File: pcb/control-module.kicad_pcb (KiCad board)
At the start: 2 copper layers, 78.7 x 69.9 mm, 175 parts, among them J1 Screw_Terminal_01x06, J2 Conn_01x07_Pin, J3 USB_C_Receptacle_USB2.0_16P, J4 Micro_SD_Card, J5 Conn_ST_STDC14, J6 Conn_Coaxial, Q1 SiS454DN, Q2 SiS454DN, SW1 SW_DIP_x04, SW2 SW_DIP_x04, U1 TPS2116DRL, U2 USBLC6-2SC6, U3 STM32U545RETxQ, U4 MS5607-02BA, U5 LSM6DSL, U6 MCP73831-2-OT, U7 MIC5504-3.3YM5, U9 STM32WL55CCUx

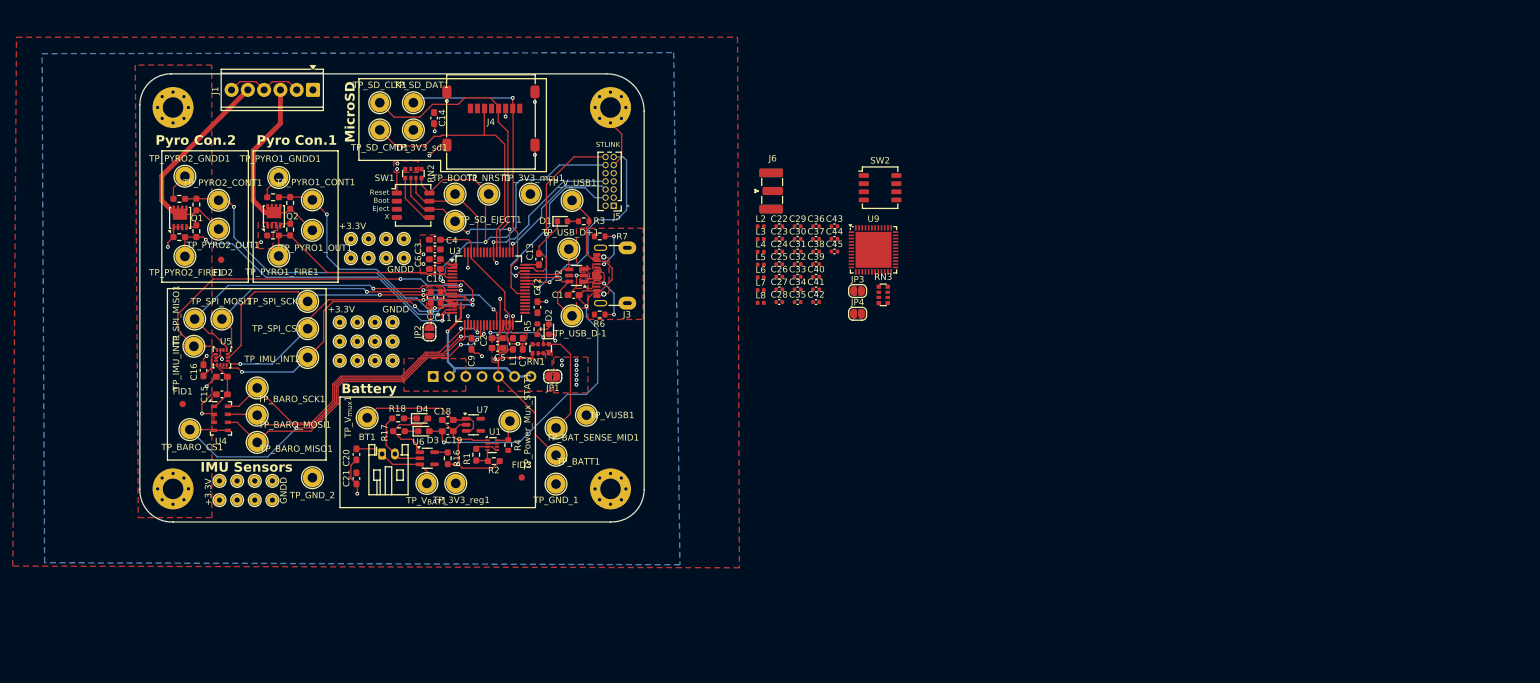
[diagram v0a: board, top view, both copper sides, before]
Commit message: Updated parts
Updated parts, most should be included at this point. Layout is not complete.
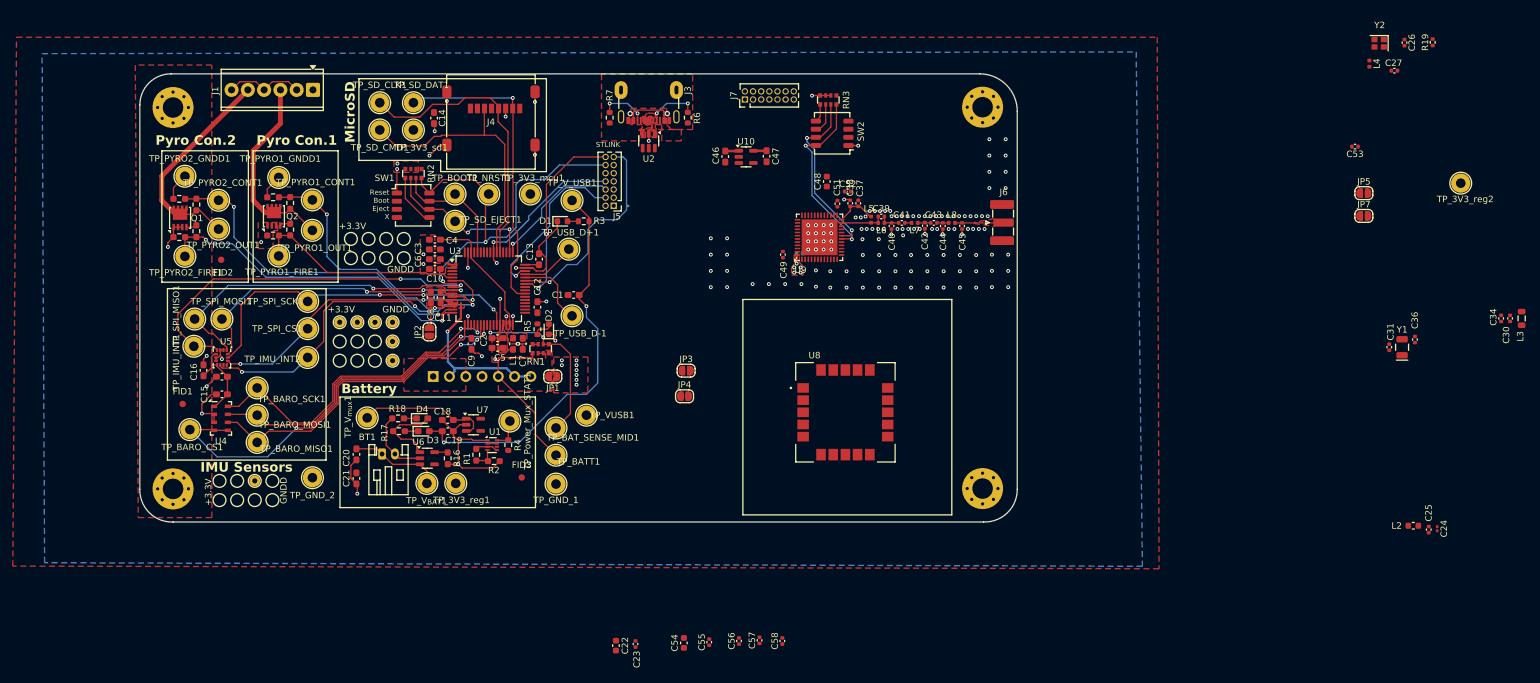
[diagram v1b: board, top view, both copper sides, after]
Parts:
- removed ? (x21): , 
- removed C28, C29, C32, C33, C35: C, Capacitor_SMD:C_0402_1005Metric
- added C46: 1uF, Capacitor_SMD:C_0603_1608Metric_Pad1.08x0.95mm_HandSolder, F.Cu at (206.7, 32.9)
- added C47: 1uF, Capacitor_SMD:C_0603_1608Metric_Pad1.08x0.95mm_HandSolder, F.Cu at (213.1, 32.9)
- added C48: 4.7uF, Capacitor_SMD:C_0603_1608Metric, F.Cu at (222.5, 36.8)
- added C49: 100nF, Capacitor_SMD:C_0402_1005Metric, F.Cu at (215.7, 48.2)
- added C50: 33pF, Capacitor_SMD:C_0402_1005Metric, B.Cu at (218.2, 48.0)
- added C51: 33pF, Capacitor_SMD:C_0402_1005Metric, F.Cu at (224.2, 40.2)
- added C52: 100nF, Capacitor_SMD:C_0402_1005Metric, F.Cu at (225.8, 38.4)
- added C53: 33pF, Capacitor_SMD:C_0402_1005Metric, F.Cu at (304.9, 31.4)
- added C54: 4.7uF, Capacitor_SMD:C_0603_1608Metric, F.Cu at (200.2, 108.8)
- added C55: 100nF, Capacitor_SMD:C_0402_1005Metric, F.Cu at (204.2, 108.7)
- added C56: 100nF, Capacitor_SMD:C_0402_1005Metric, F.Cu at (208.8, 108.5)
- added C57: 100nF, Capacitor_SMD:C_0402_1005Metric, F.Cu at (212.0, 108.4)
- added C58: 100nF, Capacitor_SMD:C_0402_1005Metric, F.Cu at (215.6, 108.5)
- added J7: Conn_ST_STDC14, Connector_PinHeader_1.27mm:PinHeader_2x07_P1.27mm_Vertical, F.Cu at (209.7, 24.0)
- added JP5: ~, Jumper:SolderJumper-2_P1.3mm_Open_RoundedPad1.0x1.5mm, F.Cu at (306.3, 38.6)
- added JP7: SolderJumper_2_Open, Jumper:SolderJumper-2_P1.3mm_Open_RoundedPad1.0x1.5mm, F.Cu at (306.3, 42.2)
- added R19: 220R, Resistor_SMD:R_0402_1005Metric, F.Cu at (317.0, 15.1)
- added TP_3V3_reg2: TestPoint, TestPoint:TestPoint_Loop_D2.54mm_Drill1.5mm_Beaded, F.Cu at (321.4, 37.0)
- added U10: MIC5504-3.3YM5, Package_TO_SOT_SMD:SOT-23-5, F.Cu at (209.9, 33.0)
- added U8: SAM-M10Q-00B, SAM M10Q:XCVR_SAM-M10Q-00B, F.Cu at (225.4, 72.8)
- added Y1: Crystal, Crystal:Crystal_SMD_G8-2Pin_3.2x1.5mm, F.Cu at (312.2, 62.6)
- added Y2: Crystal_GND23, Crystal:Crystal_SMD_SeikoEpson_FA128-4Pin_2.0x1.6mm, F.Cu at (308.7, 15.2)
- C22: value C -> 4.7uF; footprint Capacitor_SMD:C_0402_1005Metric -> Capacitor_SMD:C_0603_1608Metric
- C23, C25: value C -> 100nF
- C24: value C -> 4.7uF; footprint Capacitor_SMD:C_0402_1005Metric -> Capacitor_SMD:C_0201_0603Metric
- C26: value C -> 10pF
- C27: value C -> 220nF
- C30: value C -> 0.47uF
- C31, C36, C44, C45: value C -> 6.8pF
- C34: value C -> 33pF
- C37: value C -> 47nF
- C38, C41, C43: value C -> 68pF
- C39: value C -> 4.3pF
- C40: value C -> 15pF
- C42: value C -> 5.6pF
- L2: value L -> 600R Ferrite Bead; footprint Inductor_SMD:L_0402_1005Metric -> Inductor_SMD:L_0603_1608Metric
- L3: value L -> 15uH; footprint Inductor_SMD:L_0402_1005Metric -> Inductor_SMD:L_0805_2012Metric
- L4: value L -> 1400R Ferrite Bead
- L5: value L -> 56nH
- L6: value L -> 6.8nH
- L7, L8: value L -> 16nH
- moved L3 119.4 mm to (330.9, 58.1), turned to 90 degrees
- moved L2 112.0 mm to (314.0, 90.5), turned to 180 degrees
- moved C30 111.8 mm to (329.1, 58.1), turned to -90 degrees
- moved C24 111.4 mm to (317.7, 91.0), turned to -90 degrees
- moved C34 109.8 mm to (327.7, 58.1), turned to -90 degrees
- moved C25 109.5 mm to (316.4, 91.1), turned to -90 degrees
- moved C26 104.2 mm to (312.6, 15.1), turned to -90 degrees
- moved C27 101.9 mm to (311.1, 19.5)
- moved L4 99.4 mm to (307.1, 18.4), turned to 90 degrees
- moved C36 95.1 mm to (314.2, 61.5), turned to -90 degrees
- moved C31 93.5 mm to (310.2, 62.6), turned to -90 degrees
- moved C22 70.2 mm to (189.6, 109.2), turned to -90 degrees
- moved C23 67.1 mm to (192.7, 109.0), turned to -90 degrees
- moved H1 58.1 mm to (246.8, 84.7)
- moved H2 58.1 mm to (246.8, 25.2)
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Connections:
- net /Transmitter/BOOT0 renamed /transmitter/BOOT0_radio
- net /Transmitter/NRST renamed /transmitter/NRST_radio
- net Net-(U9-VDDRF1V55) renamed VDDRF1V55
- C22 pad 1: Net-(U9-VDDPA) -> +3.3V_radio
- C23 pad 1: Net-(U9-VDDPA) -> +3.3V_radio
- C26 pad 1: +3.3V -> /transmitter/OSC_IN
- C26 pad 2: GNDD -> Net-(C26-Pad2)
- C27 pad 1: +3.3V -> Net-(C27-Pad1)
- C39 pad 1: Net-(C39-Pad1) -> Net-(U9-RFO_HP)
- JP4 pad 1: +3.3V -> +3.3V_radio
- L2 pad 2: +3.3V -> +3.3V_radio
- L4 pad 1: Net-(U9-RFO_HP) -> Net-(C27-Pad1)
- L4 pad 2: Net-(C39-Pad1) -> /transmitter/VDD_TCXO
- L5 pad 2: Net-(C39-Pad1) -> Net-(U9-RFO_HP)
- L6 pad 1: Net-(C39-Pad1) -> Net-(U9-RFO_HP)
- RN3 pad 1: +3.3V -> +3.3V_radio
- SW2 pad 2: +3.3V -> +3.3V_radio
- U9 pad 11: +3.3V -> +3.3V_radio
- U9 pad 25: Net-(U9-VDDPA) -> +3.3V_radio
- U9 pad 26: /Transmitter/OSC_IN -> /transmitter/OSC_IN
- U9 pad 27: /Transmitter/OSC_OUT -> Net-(JP5-B)
- U9 pad 28: Net-(U9-VDDPA) -> +3.3V_radio
- U9 pad 30: unconnected-(U9-PB0-Pad30) -> /transmitter/VDD_TCXO
- U9 pad 37: +3.3V -> +3.3V_radio
- U9 pad 44: +3.3V -> +3.3V_radio
- U9 pad 46: Net-(U9-VDDPA) -> +3.3V_radio
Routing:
- net /transmitter/NRST_radio: track 0.00 -> 28.9 mm, vias 0 -> 2
- net /transmitter/BOOT0_radio: track 0.00 -> 27.6 mm, vias 0 -> 2
- net Net-(J6-In): track 0.00 -> 7.62 mm
- net Net-(U9-RFO_HP): track 0.00 -> 6.74 mm
- net Net-(U9-VR_PA): track 0.00 -> 6.53 mm
- net Net-(RN3-R3.2): track 0.00 -> 4.84 mm
- net Net-(C39-Pad2): track 0.00 -> 3.24 mm
- net Net-(RN3-R4.2): track 0.00 -> 2.87 mm
- net /MCU/USB_DN: track 14.3 -> 11.5 mm
- net /transmitter/V_{battery_radio}: track 0.00 -> 2.13 mm
- net Net-(C42-Pad1): track 0.00 -> 2.07 mm
- net +3.3V_radio: track 0.00 -> 2.07 mm
- net Net-(C43-Pad2): track 0.00 -> 1.83 mm
- net /MCU/USB_DP: track 10.4 -> 8.57 mm
- net +5V_USB: track 69.1 -> 70.9 mm
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- added copper zone on In1.Cu, net GNDD
- added copper zone on F.Cu, net Net-(J6-In)
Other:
- board size 78.7 x 69.9 mm -> 136.9 x 69.9 mm
- copper layers 2 -> 4

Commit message: Backup
Backup before board layer change from 4-2 in case of lost components
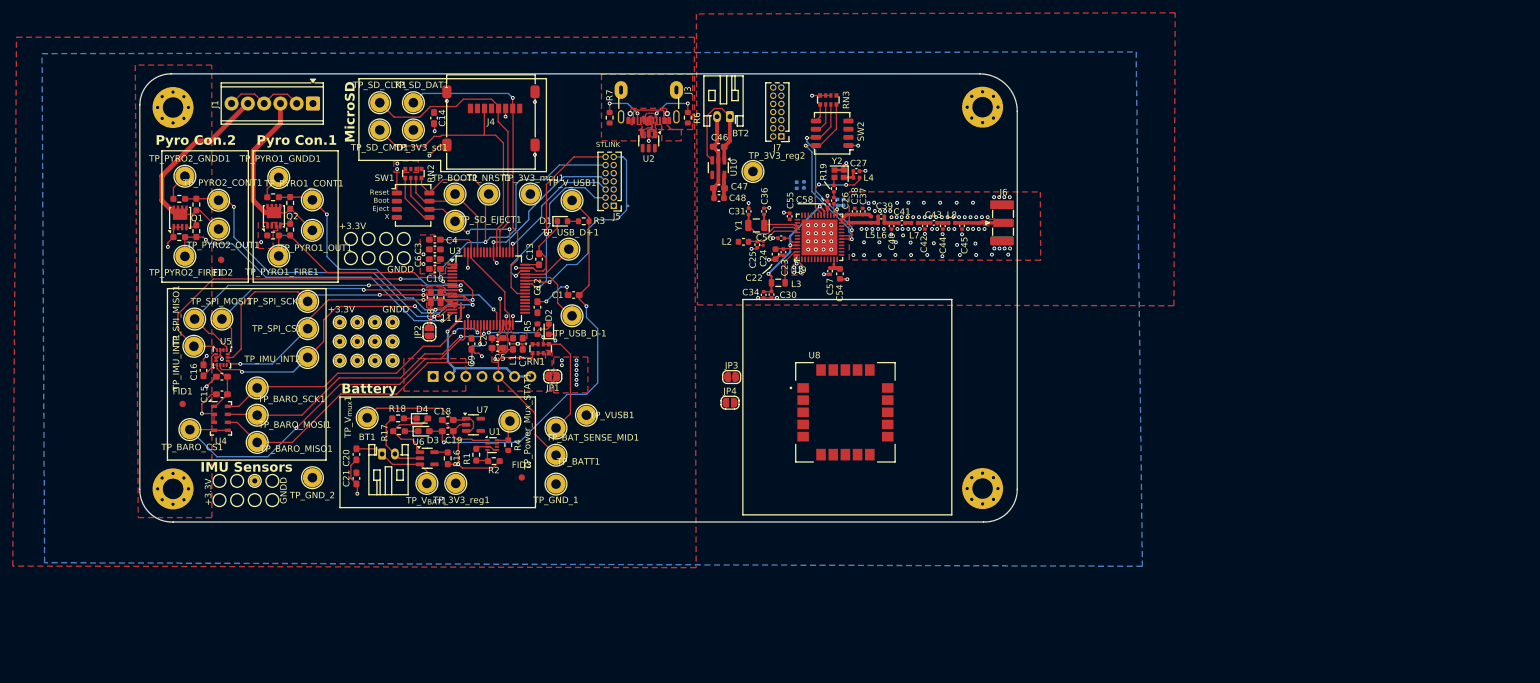
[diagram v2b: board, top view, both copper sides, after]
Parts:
- removed C53: 33pF, Capacitor_SMD:C_0402_1005Metric
- removed JP5: ~, Jumper:SolderJumper-2_P1.3mm_Open_RoundedPad1.0x1.5mm
- removed JP7: SolderJumper_2_Open, Jumper:SolderJumper-2_P1.3mm_Open_RoundedPad1.0x1.5mm
- added ?: , , F.Cu at (149.2, 61.8)
- added ?: , , F.Cu at (146.5, 64.8)
- added ?: , , F.Cu at (152.0, 64.8)
- added ?: , , F.Cu at (152.0, 61.8)
- added ?: , , F.Cu at (146.5, 61.8)
- added ?: , , F.Cu at (149.2, 64.8)
- added BT2: Battery_Cell, Connector_JST:JST_PH_S2B-PH-K_1x02_P2.00mm_Horizontal, F.Cu at (207.4, 26.7)
- C49, C51, C52: moved to B.Cu
- moved L3 116.1 mm to (214.9, 52.6), turned to 180 degrees
- moved C30 115.3 mm to (213.9, 54.4)
- moved C34 115.1 mm to (212.7, 54.5)
- moved C24 114.2 mm to (212.6, 46.5)
- moved C25 113.8 mm to (211.7, 46.6)
- moved L2 113.5 mm to (209.5, 46.2)
- moved TP_3V3_reg2 110.4 mm to (211.0, 35.2)
- moved C36 103.5 mm to (212.7, 41.5)
- moved Y1 102.5 mm to (211.5, 43.6), turned to 180 degrees
- moved C31 102.2 mm to (210.3, 41.5)
- moved R19 96.2 mm to (223.6, 37.9)
- moved C26 92.4 mm to (223.6, 39.8), turned to 90 degrees
- moved Y2 86.7 mm to (224.4, 35.6)
- moved C27 85.4 mm to (227.1, 35.1)
- moved L4 82.0 mm to (227.1, 36.2), turned to 0 degrees
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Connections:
- C51 pad 1: Net-(JP7-B) -> +3.3V_radio
- C52 pad 1: Net-(JP7-B) -> +3.3V_radio
- U9 pad 27: Net-(JP5-B) -> unconnected-(U9-OSC_OUT-Pad27)
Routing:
- net GNDD: track 123.0 -> 155.6 mm, vias 168 -> 154
- net VDDRF1V55: track 0.00 -> 20.9 mm, vias 0 -> 3
- net /transmitter/V_{battery_radio}: track 2.13 -> 19.0 mm
- net +3.3V_radio: track 2.07 -> 16.4 mm, vias 0 -> 1
- net /transmitter/VDD_TCXO: track 0.00 -> 12.4 mm, vias 0 -> 2
- net Net-(U9-PC15): track 0.00 -> 10.5 mm
- net Net-(U9-VDDA): track 0.00 -> 8.40 mm
- net Net-(U9-PC14): track 0.00 -> 7.08 mm
- net /IMU Sensors/pres_sclk: track 51.9 -> 45.6 mm
- net Net-(U9-VLXSMPS): track 0.00 -> 5.91 mm
- net /IMU Sensors/pres_mosi: track 49.4 -> 46.5 mm
- net Net-(C27-Pad1): track 0.00 -> 2.68 mm
- net /Pyro Controller 1/Out: track 30.7 -> 28.6 mm
- net /transmitter/OSC_IN: track 0.00 -> 1.81 mm
- net /IMU Sensors/pres_cs: track 61.9 -> 60.3 mm
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- added copper zone on F.Cu, net +3.3V_radio
- added copper zone on F.Cu, net Net-(U9-RFO_HP)
- removed copper zone on In1.Cu, net GNDD

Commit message: Pre-fab update
Pre fab update
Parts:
- removed ? (x6): , 
- removed C49: 100nF, Capacitor_SMD:C_0402_1005Metric
- removed J2: Conn_01x07_Pin, Connector_PinHeader_2.54mm:PinHeader_1x07_P2.54mm_Vertical
- removed TP_3V3_reg1, TP_BATT1, TP_Power_Mux_STAT1, TP_VUSB1, TP_V_{BAT}1, TP_V_{mux}1: TestPoint, TestPoint:TestPoint_Loop_D2.54mm_Drill1.5mm_Beaded
- added BATT1: TestPoint, TestPoint:TestPoint_Loop_D2.54mm_Drill1.5mm_Beaded, F.Cu at (167.7, 84.6)
- added C28: 100nF, Capacitor_SMD:C_0603_1608Metric_Pad1.08x0.95mm_HandSolder, B.Cu at (224.1, 70.9)
- added C29: 1uF, Capacitor_SMD:C_0603_1608Metric_Pad1.08x0.95mm_HandSolder, B.Cu at (222.0, 72.0)
- added C32: 4.7uF, Capacitor_SMD:C_0603_1608Metric, B.Cu at (226.1, 69.4)
- added Pwr_Mux_ST1: TestPoint, TestPoint:TestPoint_Loop_D2.54mm_Drill1.5mm_Beaded, F.Cu at (171.5, 70.9)
- added VDD3V3: TestPoint, TestPoint:TestPoint_Loop_D2.54mm_Drill1.5mm_Beaded, F.Cu at (173.4, 84.6)
- added V_{mux}1: TestPoint, TestPoint:TestPoint_Loop_D2.54mm_Drill1.5mm_Beaded, F.Cu at (170.6, 80.8)
- C50: moved to F.Cu
- JP3, JP4: moved to B.Cu
- moved FID3 73.8 mm to (248.5, 77.3)
- moved J3 62.6 mm to (193.5, 86.2), turned to 0 degrees
- moved FID2 59.6 mm to (182.3, 24.5)
- moved R6 57.7 mm to (187.4, 83.0), turned to 90 degrees
- moved R7 57.2 mm to (199.6, 83.0), turned to 90 degrees
- moved U2 48.9 mm to (193.5, 79.4), turned to 90 degrees
- moved D1 43.4 mm to (206.0, 78.6), turned to 90 degrees
- moved R3 40.6 mm to (203.9, 78.7), turned to 90 degrees
- moved +5V_USB1 34.6 mm to (198.3, 70.6)
- moved G*** 34.0 mm to (198.5, 54.0), turned to 90 degrees
- moved USB_D+1 32.8 mm to (198.2, 76.1)
- moved JP3 29.5 mm to (233.8, 53.7), turned to 180 degrees
- moved C1 29.5 mm to (197.0, 80.4), turned to 0 degrees
- moved JP4 27.4 mm to (231.2, 57.7)
- moved C21 26.6 mm to (174.8, 76.0)
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- renumbered TP_V_USB1 to +5V_USB1, TP_3V3_mcu1 to 3V3_mcu1, TP_3V3_reg2 to 3V3_reg2, TP_3V3_sd1 to 3V3_sd1, TP_BARO_CS1 to BARO_CS1, TP_BARO_MISO1 to BARO_MISO1, TP_BARO_MOSI1 to BARO_MOSI1, TP_BARO_SCK1 to BARO_SCK1, TP_BAT_SENSE_MID1 to BAT_SENSE_MID1, TP_BOOT1 to BOOT1, TP_PYRO2_GNDD1 to GNDD1, TP_IMU_INT1 to IMU_INT1, TP_IMU_INT2 to IMU_INT2, TP_NRST1 to NRST1, TP_PYRO1_CONT1 to PYRO1_CONT1, TP_PYRO1_FIRE1 to PYRO1_FIRE1, TP_PYRO1_GNDD1 to PYRO1_GNDD1, TP_PYRO1_OUT1 to PYRO1_OUT1, TP_PYRO2_CONT1 to PYRO2_CONT1, TP_PYRO2_FIRE1 to PYRO2_FIRE1, TP_PYRO2_OUT1 to PYRO2_OUT1, TP_SD_CLK1 to SD_CLK1, TP_SD_CMD1 to SD_CMD1, TP_SD_DAT1 to SD_DAT1, TP_SD_EJECT1 to SD_EJECT1, TP_SPI_CS1 to SPI_CS1, TP_SPI_MISO1 to SPI_MISO1, TP_SPI_MOSI1 to SPI_MOSI1, TP_SPI_SCK1 to SPI_SCK1, TP_USB_D+1 to USB_D+1, TP_USB_D-1 to USB_D-1
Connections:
- BT1 pad 1: /Battery/V_{BAT} -> V_{BAT}
- C20 pad 1: /Battery/V_{BAT} -> V_{BAT}
- J5 pad 13: /MCU/MCU_RX -> /MCU/MCU_TX
- J5 pad 14: /MCU/MCU_TX -> /MCU/MCU_RX
- J7 pad 12: /STLink/NRST_radio -> /NRST_radio
- J7 pad 13: /STLink/STLink_radio -> /radio_RX
- J7 pad 14: /STLink/STLink_radio -> /radio_TX
- J7 pad 3: +3.3V -> +3.3V_radio
- J7 pad 4: /STLink/SWDIO_radio -> /SWDIO_radio
- J7 pad 6: /STLink/SWCLK_radio -> /SWCLK_radio
- J7 pad 8: /STLink/SWO_radio -> /SWO_radio
- JP3 pad 1: GNDD -> /Ublox_GPS_module/GPS_TX
- JP3 pad 2: GNDA -> /radio_TX
- JP4 pad 1: +3.3V_radio -> /radio_RX
- JP4 pad 2: VDDA -> /Ublox_GPS_module/GPS_RX
- R1 pad 2: /V_USB -> +5V_USB
- RN1 pad 1: +BATT -> V_{BAT}
- RN3 pad 8: /transmitter/NRST_radio -> /NRST_radio
- SW2 pad 8: /transmitter/NRST_radio -> /NRST_radio
- U1 pad 2: /V_{mux} -> /Battery/V_{mux}
- U1 pad 3: /V_USB -> +5V_USB
- U1 pad 5: /V_USB -> +5V_USB
- U1 pad 6: /V_{BAT} -> V_{BAT}
- U1 pad 7: /V_{mux} -> /Battery/V_{mux}
- U3 pad 51: unconnected-(U3-PC10-Pad51) -> /SPI3_SCK
- U3 pad 52: unconnected-(U3-PC11-Pad52) -> /SPI3_MISO
- U3 pad 56: unconnected-(U3-PB4-Pad56) -> /SPI3_CS
- U3 pad 57: unconnected-(U3-PB5-Pad57) -> /SPI3_MOSI
- U6 pad 3: /Battery/V_{BAT} -> V_{BAT}
- U6 pad 4: /Battery/V_USB -> +5V_USB
- U8 pad 1: GND -> GNDD
- U8 pad 10: GND -> GNDD
- U8 pad 11: GND -> GNDD
- U8 pad 13: unconnected-(U8-TXD-Pad13) -> /Ublox_GPS_module/GPS_TX
- U8 pad 14: unconnected-(U8-RXD-Pad14) -> /Ublox_GPS_module/GPS_RX
- U8 pad 15: GND -> GNDD
- U8 pad 16: GND -> GNDD
- U8 pad 17: unconnected-(U8-VCC-Pad17) -> +3.3V_radio
- U8 pad 18: unconnected-(U8-~{RESET}-Pad18) -> +3.3V_radio
- U8 pad 2: unconnected-(U8-V_IO-Pad2) -> +3.3V_radio
- U8 pad 20: GND -> GNDD
- U8 pad 3: unconnected-(U8-V_BCKP-Pad3) -> +3.3V_radio
- U8 pad 4: GND -> GNDD
- U8 pad 5: GND -> GNDD
- U8 pad 6: GND -> GNDD
- U8 pad 7: unconnected-(U8-TIMEPULSE-Pad7) -> /Ublox_GPS_module/TIMEPULSE_OUT
- U9 pad 1: unconnected-(U9-PB3-Pad1) -> /SWO_radio
- U9 pad 13: unconnected-(U9-PA5-Pad13) -> /Ublox_GPS_module/TIMEPULSE_OUT
- U9 pad 18: /transmitter/NRST_radio -> /NRST_radio
- U9 pad 2: unconnected-(U9-PB4-Pad2) -> /SPI3_MISO
- U9 pad 3: unconnected-(U9-PB5-Pad3) -> /SPI3_MOSI
- U9 pad 36: unconnected-(U9-PA13-Pad36) -> /SWDIO_radio
- U9 pad 4: unconnected-(U9-PB6-Pad4) -> /radio_RX
- U9 pad 42: unconnected-(U9-PA14-Pad42) -> /SWCLK_radio
- U9 pad 5: unconnected-(U9-PB7-Pad5) -> /radio_TX
- U9 pad 7: unconnected-(U9-PA0-Pad7) -> /SPI3_CS
- U9 pad 8: unconnected-(U9-PA1-Pad8) -> /SPI3_SCK
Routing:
- net /SPI3_MOSI: track 0.00 -> 76.7 mm, vias 0 -> 4
- net /SPI3_CS: track 0.00 -> 72.4 mm, vias 0 -> 4
- net /SPI3_MISO: track 0.00 -> 68.0 mm, vias 0 -> 4
- net /SPI3_SCK: track 0.00 -> 66.7 mm, vias 0 -> 2
- net /NRST_radio: track 0.00 -> 63.7 mm, vias 0 -> 3
- net /Ublox_GPS_module/TIMEPULSE_OUT: track 0.00 -> 56.3 mm, vias 0 -> 2
- net V_{BAT}: track 0.00 -> 50.1 mm, vias 0 -> 9
- net GNDD: track 155.6 -> 113.8 mm, vias 154 -> 345
- net /radio_RX: track 0.00 -> 37.4 mm, vias 0 -> 2
- net /radio_TX: track 0.00 -> 36.1 mm, vias 0 -> 2
- net /MCU/USB_DP: track 8.57 -> 41.7 mm
- net +3.3V_radio: track 16.4 -> 47.5 mm, vias 1 -> 6
- net /MCU/USB_DN: track 11.5 -> 41.3 mm
- net /transmitter/NRST_radio: track 28.9 -> 0.00 mm, vias 2 -> 0
- net /Ublox_GPS_module/GPS_TX: track 0.00 -> 25.7 mm, vias 0 -> 1
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- added copper zone on F.Cu, net +5V_USB
- removed copper zone on F.Cu, net /V_USB
- removed copper zone on F.Cu, net Net-(J1-Pin_2)
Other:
- copper layers 4 -> 2
- board text added: "Spring 2026"
- board text added: "X X 3V3 GND"
- board text added: "X X BOOT NRST"
- board text removed: "BAT+"
- board text removed: "GNDA"
